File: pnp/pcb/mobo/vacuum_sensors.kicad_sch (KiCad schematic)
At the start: 18 parts, among them J33 I2C_AUX, U2 XGZP6857D, U3 XGZP6857D, U4 PCA9545A

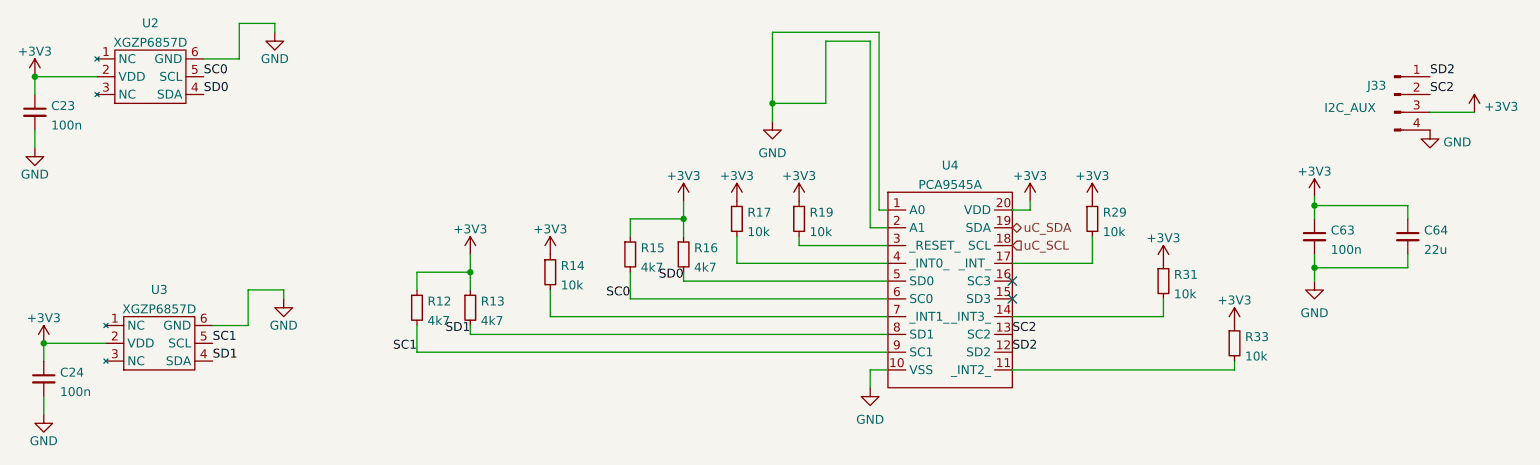
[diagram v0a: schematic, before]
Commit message: tweak PN of mobo
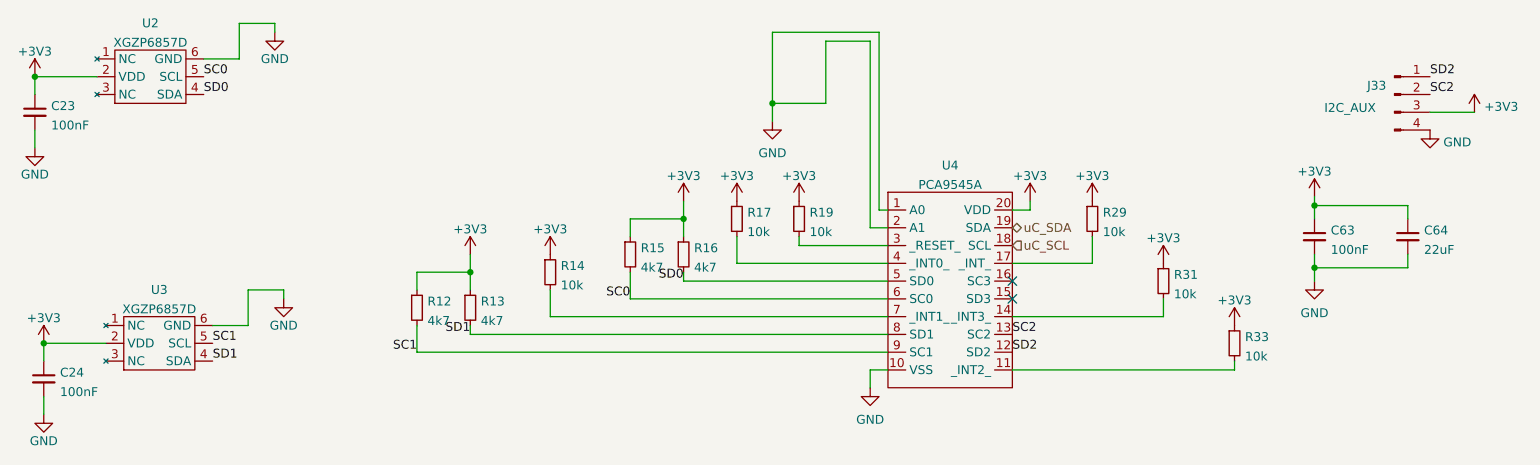
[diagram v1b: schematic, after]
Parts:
- C23, C24, C63: value 100n -> 100nF
- C64: value 22u -> 22uF
- J33: LCSC (none) -> C2691448
- U2, U3: LCSC (none) -> DNP
- U4: LCSC (none) -> C129515
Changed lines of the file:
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@@
+      (effects (font (size 1.27 1.27)) hide)
+    )
+    (property "LCSC" "C2691448" (at 256.54 86.36 0)
       (effects (font (size 1.27 1.27)) hide)
     )
@@
       (effects (font (size 1.27 1.27)) (justify left))
     )
-    (property "Value" "100n" (at 247.4341 108.5529 0)
+    (property "Value" "100nF" (at 247.4341 108.5529 0)
       (effects (font (size 1.27 1.27)) (justify left))
     )
@@
       (effects (font (size 1.27 1.27)) (justify left))
     )
-    (property "Value" "22u" (at 260.7691 108.5529 0)
+    (property "Value" "22uF" (at 260.7691 108.5529 0)
       (effects (font (size 1.27 1.27)) (justify left))
     )
@@
       (effects (font (size 1.27 1.27)) (justify left))
     )
-    (property "Value" "100n" (at 64.5541 90.7729 0)
+    (property "Value" "100nF" (at 64.5541 90.7729 0)
       (effects (font (size 1.27 1.27)) (justify left))
     )
@@
     )
     (property "Digikey" "568-1865-1-ND" (at 193.04 128.27 0)
+      (effects (font (size 1.27 1.27)) hide)
+    )
+    (property "LCSC" "C129515" (at 193.04 128.27 0)
       (effects (font (size 1.27 1.27)) hide)
     )
@@
       (effects (font (size 1.27 1.27)) (justify left))
     )
-    (property "Value" "100n" (at 65.8241 128.8729 0)
+    (property "Value" "100nF" (at 65.8241 128.8729 0)
       (effects (font (size 1.27 1.27)) (justify left))
     )
@@
     )
     (property "Notes" "Must at least cover 0 - 1 bar / 0 - 0.1 MPa / 0 - 15 PSI" (at 80.01 121.92 0)
+      (effects (font (size 1.27 1.27)) hide)
+    )
+    (property "LCSC" "DNP" (at 80.01 121.92 0)
       (effects (font (size 1.27 1.27)) hide)
     )
@@
       (effects (font (size 1.27 1.27)) hide)
     )
+    (property "LCSC" "DNP" (at 78.74 83.82 0)
+      (effects (font (size 1.27 1.27)) hide)
+    )
